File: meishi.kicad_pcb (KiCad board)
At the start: 2 copper layers, 90.7 x 55 mm, 31 parts, among them J1 USB_B_Micro, J2 Conn_01x05, SW1 SW_Push, SW11 PG1350_Socket, SW12 PG1350_Socket, SW13 PG1350_Socket, SW14 PG1350_Socket, SW15 PG1350_Socket, SW2 SW_DIP_x01, SW21 PG1350_Socket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

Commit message: fix physical collision of D1
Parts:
- moved D2 4.53 mm to (161.0, 126.9), turned to 270 degrees
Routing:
- net VBUS: track 15.1 -> 20.7 mm
- net Net-(C2-Pad1): track 9.42 -> 4.70 mm
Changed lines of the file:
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@@
     (thickness 1.6)
     (drawings 14)
-    (tracks 419)
+    (tracks 420)
     (zones 0)
     (modules 31)
@@
   )
   (module Diode_SMD:D_SOD-323 (layer B.Cu)
-    (at 157.05 129.09 180)
+    (at 161.02 126.9 270)
     (descr SOD-323)
     (tags SOD-323)
     (attr smd)
-    (fp_text reference D2 (at 0 1.85 180) (layer B.SilkS)
-      (effects (font (size 1 1) (thickness 0.15)) (justify mirror))
-    )
-    (fp_text value D_Schottky_Small (at 0.1 -1.9 180) (layer B.Fab)
-      (effects (font (size 1 1) (thickness 0.15)) (justify mirror))
-    )
-    (fp_text user %R (at 0 1.85 180) (layer B.Fab)
+    (fp_text reference D2 (at 0 1.85 270) (layer B.SilkS)
+      (effects (font (size 1 1) (thickness 0.15)) (justify mirror))
+    )
+    (fp_text value D_Schottky_Small (at 0.1 -1.9 270) (layer B.Fab)
+      (effects (font (size 1 1) (thickness 0.15)) (justify mirror))
+    )
+    (fp_text user %R (at 0 1.85 270) (layer B.Fab)
       (effects (font (size 1 1) (thickness 0.15)) (justify mirror))
     )
@@
     (fp_line (start -1.5 -0.85) (end 1.05 -0.85) (layer B.SilkS) (width 0.12))
     (fp_line (start -1.5 0.85) (end 1.05 0.85) (layer B.SilkS) (width 0.12))
-    (pad 1 smd rect (at -1.05 0 180) (size 0.6 0.45) (layers B.Cu B.Paste B.Mask)
+    (pad 1 smd rect (at -1.05 0 270) (size 0.6 0.45) (layers B.Cu B.Paste B.Mask)
       (net 3 "Net-(C2-Pad1)"))
-    (pad 2 smd rect (at 1.05 0 180) (size 0.6 0.45) (layers B.Cu B.Paste B.Mask)
+    (pad 2 smd rect (at 1.05 0 270) (size 0.6 0.45) (layers B.Cu B.Paste B.Mask)
       (net 7 VBUS))
     (model ${KISYS3DMOD}/Diode_SMD.3dshapes/D_SOD-323.wrl
@@
   (segment (start 152.72 130.92) (end 152.72 130.354315) (width 0.25) (layer F.Cu) (net 2))
   (segment (start 152.72 128.3) (end 152.157499 127.737499) (width 0.25) (layer F.Cu) (net 2))
-  (segment (start 160.66 125.06) (end 160.66 124.11) (width 0.5) (layer B.Cu) (net 3))
-  (segment (start 160.66 127.645002) (end 160.66 125.06) (width 0.5) (layer B.Cu) (net 3))
-  (segment (start 159.215002 129.09) (end 160.66 127.645002) (width 0.5) (layer B.Cu) (net 3))
-  (segment (start 158.1 129.09) (end 159.215002 129.09) (width 0.5) (layer B.Cu) (net 3))
   (segment (start 160.6175 124.0675) (end 160.66 124.11) (width 0.5) (layer B.Cu) (net 3))
   (segment (start 157.95 124.0675) (end 160.6175 124.0675) (width 0.5) (layer B.Cu) (net 3))
+  (segment (start 160.72 124.17) (end 160.66 124.11) (width 0.5) (layer B.Cu) (net 3))
+  (segment (start 161.02 124.47) (end 160.66 124.11) (width 0.5) (layer B.Cu) (net 3))
+  (segment (start 161.02 125.85) (end 161.02 124.47) (width 0.5) (layer B.Cu) (net 3))
   (segment (start 137.387499 109.4525) (end 137.724314 109.115685) (width 0.25) (layer B.Cu) (net 4))
   (segment (start 135.39 109.4525) (end 137.387499 109.4525) (width 0.25) (layer B.Cu) (net 4))
@@
   (segment (start 152.099999 122.229999) (end 153.21 123.34) (width 0.5) (layer B.Cu) (net 7))
   (segment (start 154.3275 129.09) (end 154.2975 129.06) (width 0.5) (layer B.Cu) (net 7))
-  (segment (start 156 129.09) (end 154.3275 129.09) (width 0.5) (layer B.Cu) (net 7))
   (segment (start 153.2275 127.19) (end 153.21 127.19) (width 0.5) (layer B.Cu) (net 7))
   (segment (start 154.2975 128.26) (end 153.2275 127.19) (width 0.5) (layer B.Cu) (net 7))
   (segment (start 154.2975 129.06) (end 154.2975 128.26) (width 0.5) (layer B.Cu) (net 7))
   (segment (start 153.21 123.34) (end 153.21 127.19) (width 0.5) (layer B.Cu) (net 7))
+  (segment (start 161.02 128.025) (end 161.02 127.95) (width 0.5) (layer B.Cu) (net 7))
+  (segment (start 159.985 129.06) (end 161.02 128.025) (width 0.5) (layer B.Cu) (net 7))
+  (segment (start 154.2975 129.06) (end 159.985 129.06) (width 0.5) (layer B.Cu) (net 7))
   (segment (start 140.98 129.947919) (end 140.98 131.15) (width 0.25) (layer B.Cu) (net 9))
   (segment (start 144.365911 126.562008) (end 140.98 129.947919) (width 0.25) (layer B.Cu) (net 9))

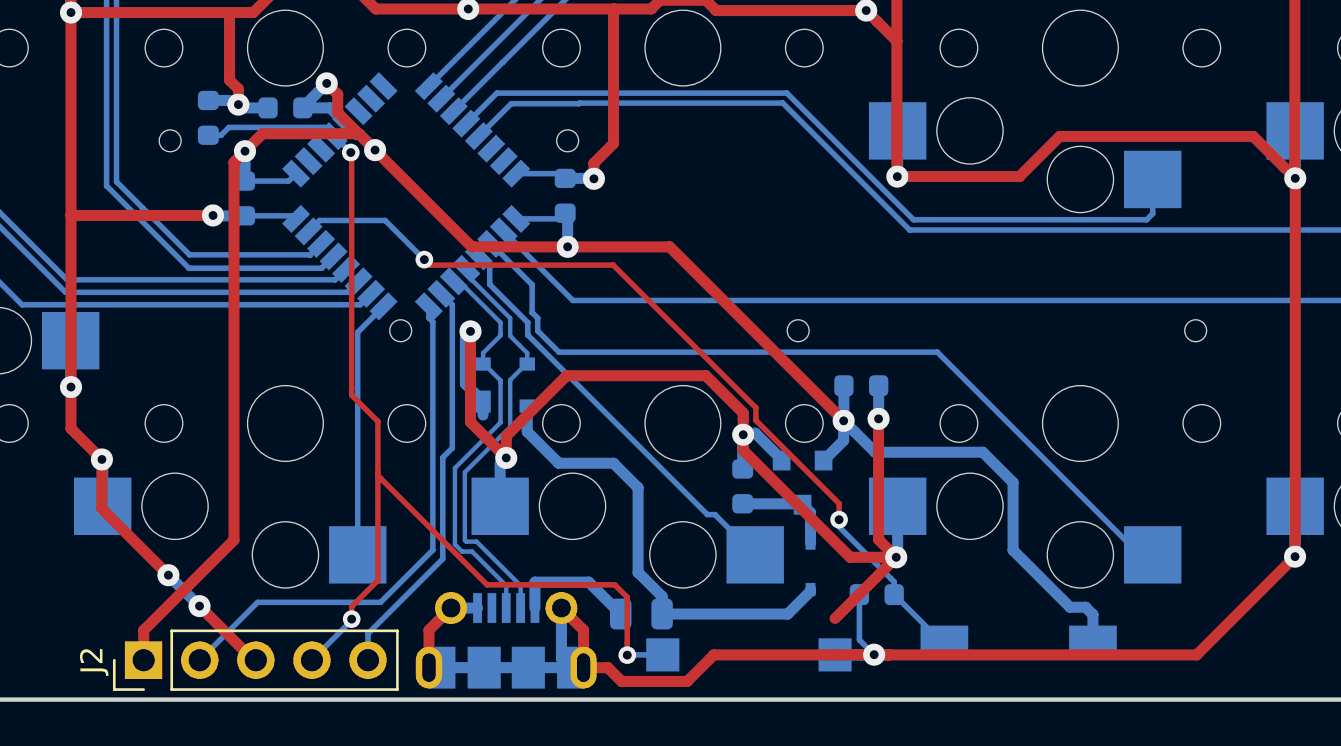
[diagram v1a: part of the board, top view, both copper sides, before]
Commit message: fix component layout
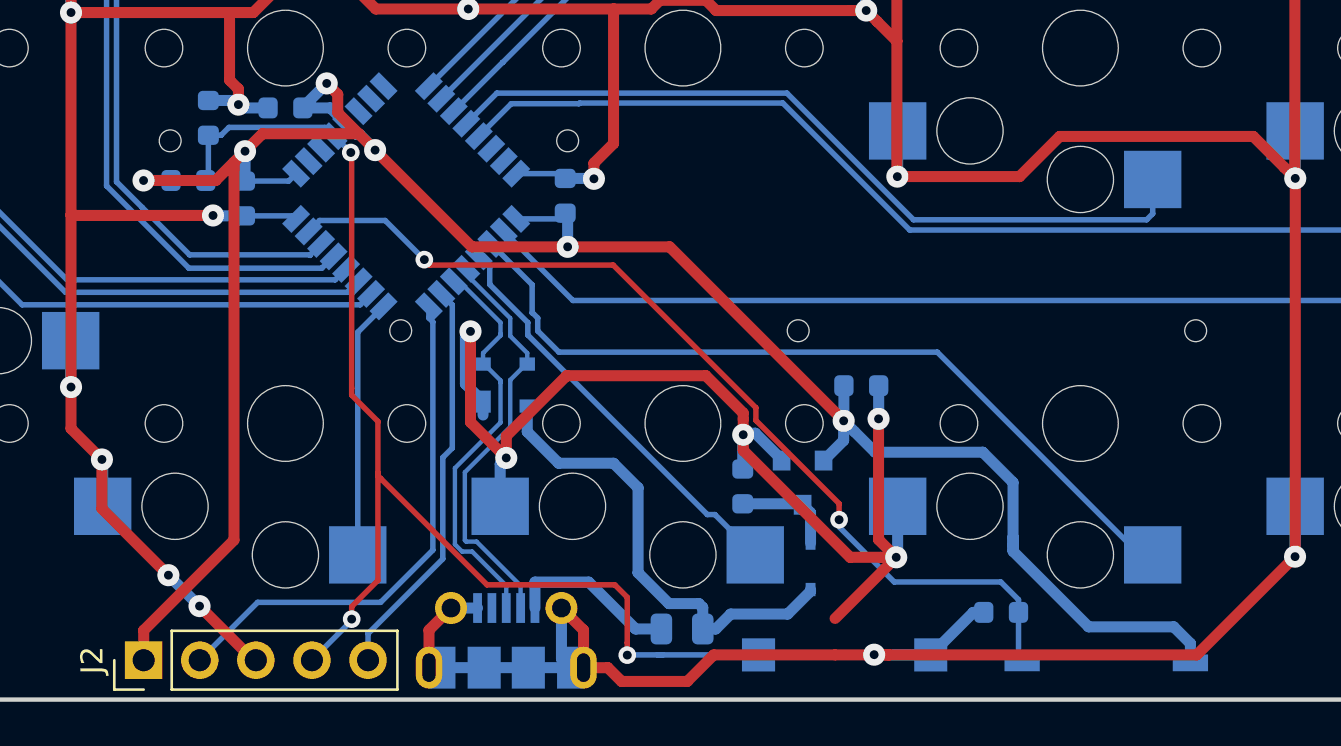
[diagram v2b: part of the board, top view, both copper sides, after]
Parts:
- added R1001: 10k, Resistor_SMD:R_0603_1608Metric, B.Cu at (132.8, 109.4)
- C1: value C_Small -> 100n
- R1: value R_Small -> 100k
- SW2: footprint Button_Switch_SMD:SW_DIP_SPSTx01_Slide_6.7x4.1mm_W6.73mm_P2.54mm_LowProfile_JPin -> Button_Switch_SMD:SW_DIP_SPSTx01_Slide_Copal_CHS-01B_W7.62mm_P1.27mm
- moved R1 5.69 mm to (169.7, 129.0)
- moved SW1 4.33 mm to (162.6, 130.9)
- moved SW2 4.12 mm to (174.4, 131.3)
- moved F1 1.96 mm to (155.2, 129.7)
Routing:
- net VDD: track 95.6 -> 106.6 mm, vias 5 -> 6
- net NRST: track 49.7 -> 56.4 mm
- net BOOT0: track 38.1 -> 43.3 mm
- net Net-(F1-Pad2): track 5.66 -> 7.78 mm
- net GND: track 339.1 -> 340.1 mm
- net VBUS: track 20.7 -> 21.3 mm

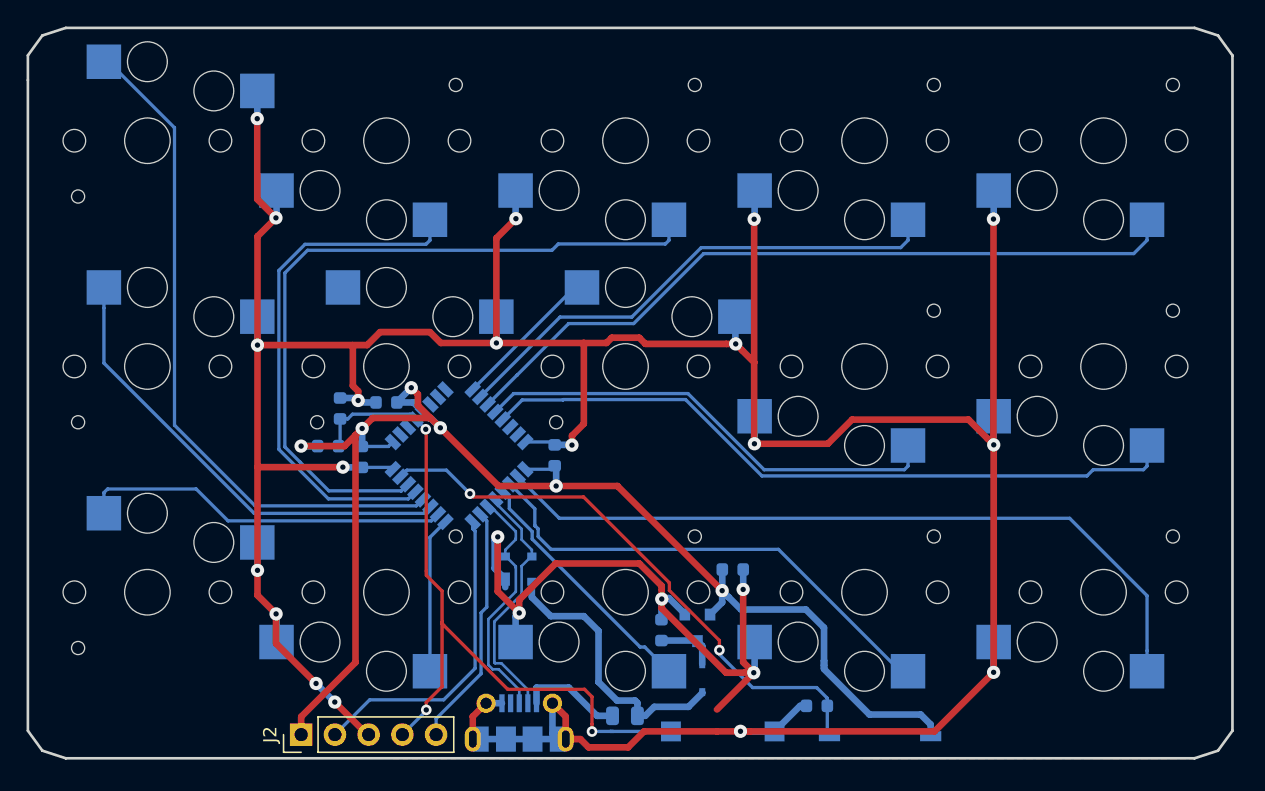
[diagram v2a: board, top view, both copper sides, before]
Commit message: fix unconnected SW22 to PA2 silk layer fix
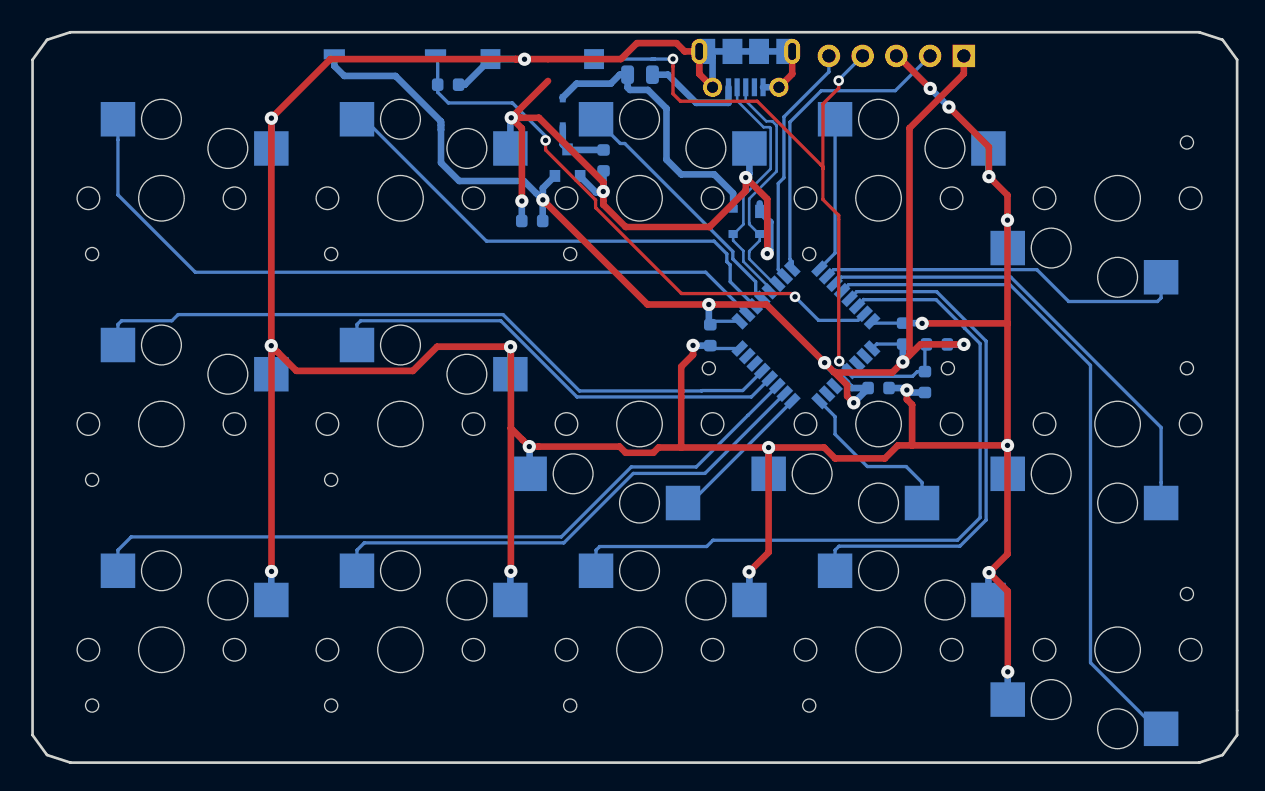
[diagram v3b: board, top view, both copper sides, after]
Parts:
- J2: moved to B.Cu
- moved SW11 82.5 mm to (192.3, 124.8), turned to 0 degrees
- moved SW15 80.6 mm to (120.3, 124.8), turned to 180 degrees
- moved SW31 78.9 mm to (192.3, 90.8), turned to 0 degrees
- moved SW35 76.9 mm to (120.3, 90.8), turned to 180 degrees
- moved SW21 73.2 mm to (192.3, 107.8), turned to 0 degrees
- moved J2 71.4 mm to (180.7, 80.0)
- moved SW25 71.1 mm to (120.3, 107.8), turned to 180 degrees
- moved SW2 63.5 mm to (137.1, 79.9), turned to 180 degrees
- moved R1 54.4 mm to (141.9, 82.2), turned to 0 degrees
- moved SW12 53.3 mm to (174.3, 124.8), turned to 180 degrees
- moved SW1 52.4 mm to (149.0, 80.3), turned to 180 degrees
- moved J1 52.2 mm to (164.3, 80.9), turned to 0 degrees
- moved SW14 51.9 mm to (138.3, 124.8), turned to 180 degrees
- moved F1 48.3 mm to (156.3, 81.5), turned to 0 degrees
- moved SW32 47.5 mm to (174.3, 90.8), turned to 180 degrees
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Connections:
- U1 pad 8: Net-(U1-Pad8) -> SW22
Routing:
- net SW22: track 0.00 -> 12.6 mm
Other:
- outline, holes or cut-outs redrawn

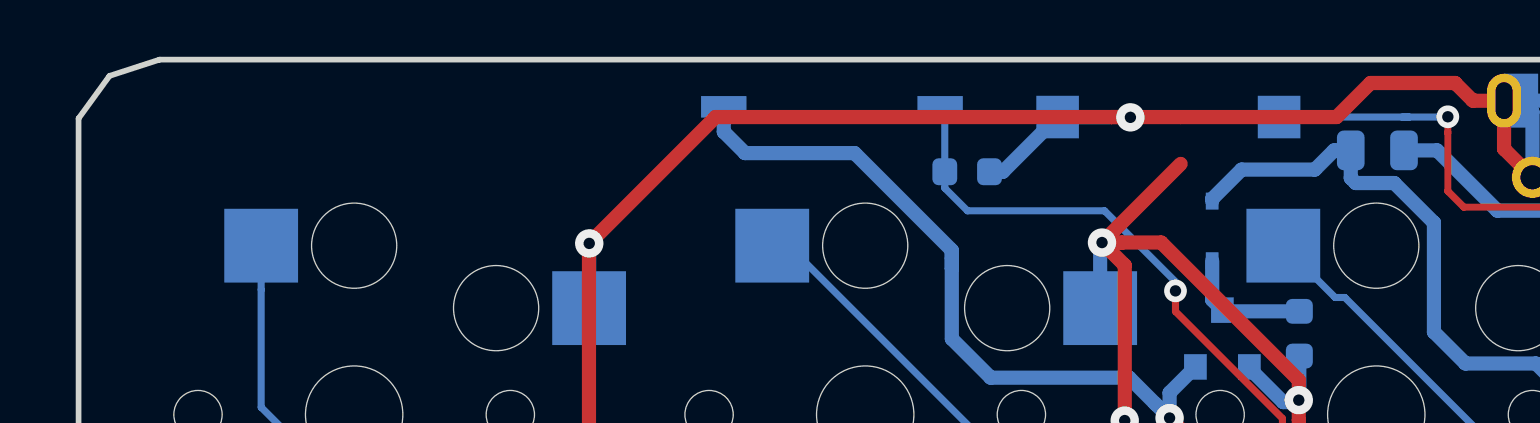
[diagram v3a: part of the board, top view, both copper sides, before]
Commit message: arrange silkscreen
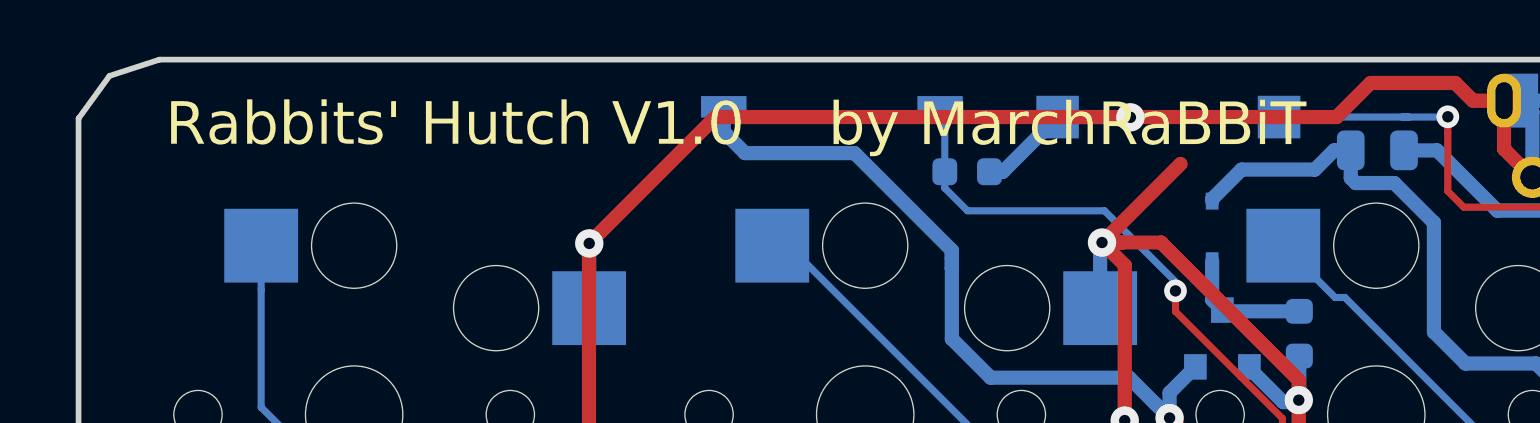
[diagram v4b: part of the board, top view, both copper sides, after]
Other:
- board text added: "Rabbits' Hutch V1.0"
- board text added: "by MarchRaBBiT"
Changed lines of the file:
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@@
   (general
     (thickness 1.6)
-    (drawings 14)
+    (drawings 16)
     (tracks 444)
     (zones 0)
@@
     )
   )
+  (gr_text "by MarchRaBBiT\n" (at 145.41282 80.53926) (layer F.SilkS)
+    (effects (font (size 1.5 1.5) (thickness 0.3)))
+  )
+  (gr_text "Rabbits' Hutch V1.0" (at 123.84822 80.5291) (layer F.SilkS)
+    (effects (font (size 1.5 1.5) (thickness 0.3)))
+  )
   (gr_text "Rabbits' hutch" (at 191.3368 80.93272) (layer B.SilkS)

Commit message: make changes
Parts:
- removed J1: USB_B_Micro, Connector_USB:USB_Micro-B_Molex-105017-0001
- added J1001: E8124-015-01, random-keyboard-parts:SparkFun_15111, B.Cu at (95.1, 35.8)
- added J3: Conn_01x04, Connector_JST:JST_SH_SM04B-SRSS-TB_1x04-1MP_P1.00mm_Horizontal, B.Cu at (113.2, 34.8)
- added R1001: 5.1k, DigiKey:0603, B.Cu at (91.2, 59.0)
- added R1002: 5.1k, DigiKey:0603, B.Cu at (95.7, 59.3)
- added R2: R_Small, DigiKey:0603, B.Cu at (140.6, 39.1)
- added R3: R_Small, Resistor_SMD:R_0603_1608Metric, B.Cu at (142.0, 40.7)
- added R4: 39k, Resistor_SMD:R_0603_1608Metric, B.Cu at (99.2, 59.8)
- added R5: 68k, Resistor_SMD:R_0603_1608Metric, B.Cu at (104.5, 56.3)
- C1, C2, C4: footprint Capacitor_SMD:C_0603_1608Metric -> DigiKey:0603
- C3, C5, C6: value 1n -> 100n; footprint Capacitor_SMD:C_0603_1608Metric -> DigiKey:0603
- R1: footprint Resistor_SMD:R_0603_1608Metric -> DigiKey:0603
- R6: renamed from R1001; footprint Resistor_SMD:R_0603_1608Metric -> DigiKey:0603
- U1: value STM32F042K4Tx -> STM32F042K6U6; footprint Package_QFP:LQFP-32_7x7mm_P0.8mm -> DigiKey:QFN-32-1EP_5x5mm
- moved SW11 160.7 mm to (50.0, 50.0)
- moved SW21 148.0 mm to (50.0, 67.0)
- moved SW31 142.5 mm to (50.0, 84.0)
- moved SW12 130.0 mm to (68.0, 50.0), turned to 0 degrees
- moved SW22 113.8 mm to (68.0, 67.0)
- moved SW32 106.5 mm to (68.0, 84.0), turned to 0 degrees
- moved SW13 102.6 mm to (86.0, 50.0), turned to 0 degrees
- moved C1 83.5 mm to (98.2, 79.3), turned to 225 degrees
- moved C6 82.4 mm to (97.2, 77.5), turned to 315 degrees
- moved SW14 82.3 mm to (104.0, 50.0), turned to 0 degrees
- moved SW23 81.3 mm to (86.0, 67.0)
- moved C5 80.9 mm to (98.9, 75.7), turned to 315 degrees
- moved U1 79.9 mm to (93.7, 74.0)
- moved C2 78.2 mm to (80.7, 59.6)
- moved C4 78.2 mm to (75.3, 64.1)
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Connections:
- F1 pad 2: Net-(F1-Pad2) -> VBUS
- U1 pad 15: Net-(U1-Pad15) -> VBUS_Sense
- U1 pad 16: GND -> Net-(U1-Pad16)
- U1 pad 2: Net-(U1-Pad2) -> I2C1_SDA
- U1 pad 3: Net-(U1-Pad3) -> I2C1_SCL
- U1 pad 31: BOOT0 -> Net-(U1-Pad31)
- U1 pad 32: GND -> BOOT0
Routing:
- net GND: track 340.1 -> 0.00 mm, vias 24 -> 0
- net VDD: track 106.6 -> 0.00 mm, vias 6 -> 0
- net SW35: track 56.8 -> 0.00 mm
- net NRST: track 56.4 -> 0.00 mm, vias 3 -> 0
- net SW15: track 56.3 -> 0.00 mm
- net SW13: track 55.5 -> 0.00 mm
- net SW25: track 53.4 -> 0.00 mm
- net SW11: track 51.2 -> 0.00 mm
- net BOOT0: track 43.3 -> 0.00 mm, vias 2 -> 0
- net SW12: track 39.4 -> 0.00 mm
- net SW14: track 38.6 -> 0.00 mm
- net SW34: track 36.9 -> 0.00 mm
- net SW24: track 35.7 -> 0.00 mm
- net SW21: track 35.2 -> 0.00 mm
- net SW31: track 28.0 -> 0.00 mm
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- removed copper zone on F.Cu, net GND
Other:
- board size 90.7 x 55 mm -> 91.2 x 57.5 mm
